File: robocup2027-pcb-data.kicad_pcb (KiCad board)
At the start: 4 copper layers, 83 x 117 mm, 52 parts, among them M5 Motor_Servo, M6 Motor_Servo, Q1 BPW40, Q2 BPW40, U1 ESP32-DEVKITC-32E

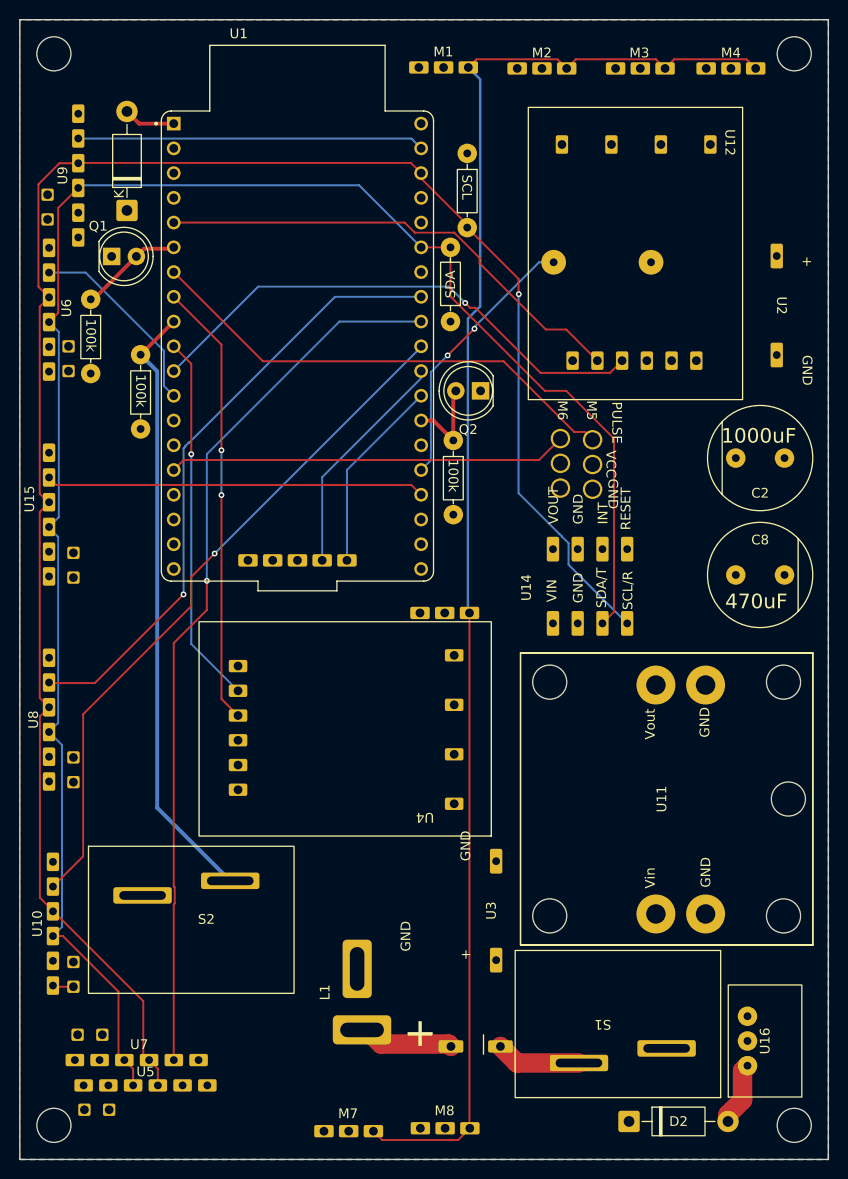
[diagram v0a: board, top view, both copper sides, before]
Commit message: fix: conflict between switches and cables
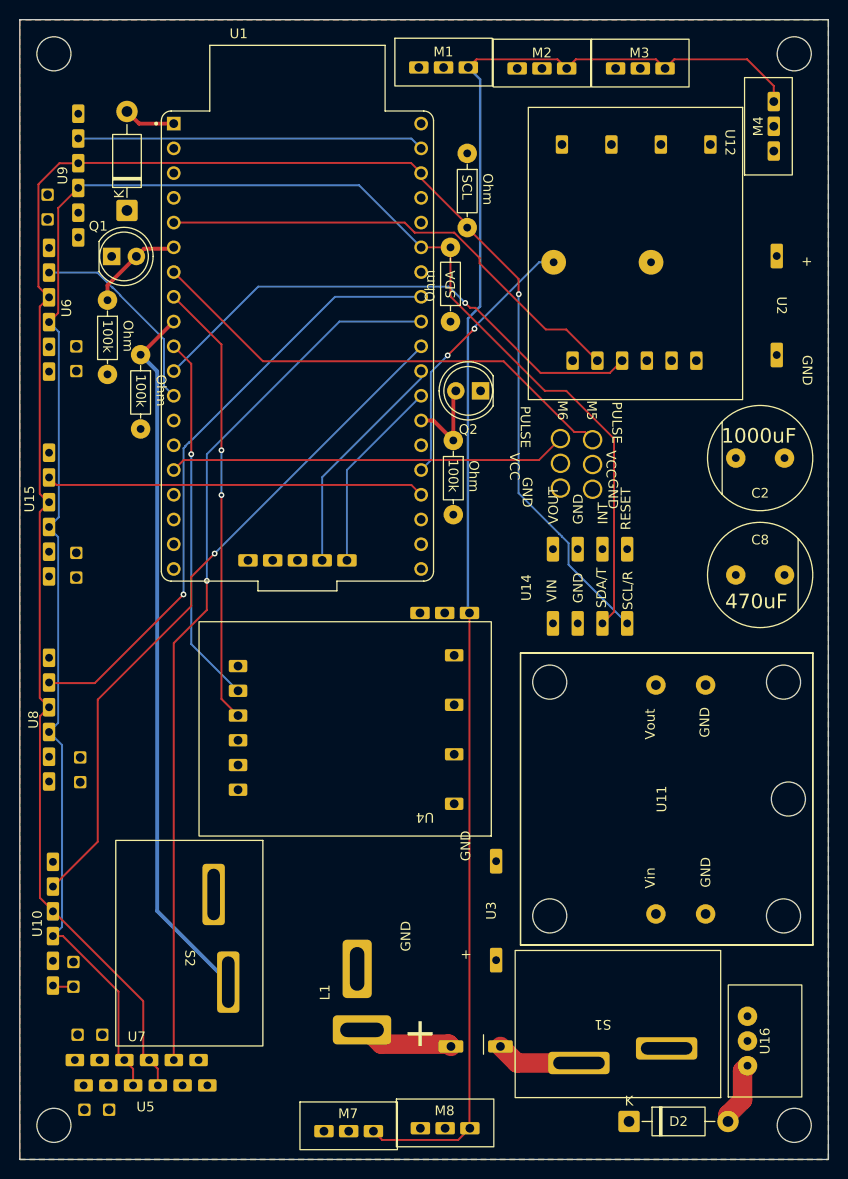
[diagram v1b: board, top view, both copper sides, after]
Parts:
- moved M4 7.39 mm to (167.4, 43.9), turned to 90 degrees
- moved S2 2.41 mm to (107.4, 127.8), turned to -90 degrees
- moved R4 1.73 mm to (99.0, 65.6)
- moved C3 0.80 mm to (95.8, 67.8)
- moved C5 0.70 mm to (96.2, 110.0)
- moved C4 0.30 mm to (95.8, 89.0)
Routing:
- net Net-(U1-IO25): track 62.6 -> 73.0 mm
- net STS3032_signal: track 152.6 -> 156.8 mm
- net photoresistor_1: track 10.7 -> 9.94 mm
- net XSHUT1: track 20.1 -> 20.9 mm

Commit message: remove: 6v voltmeter and Motor conector
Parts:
- removed M4: ~, robo:sts3032
- removed U2: ~, robo:voltmeter
- moved M1 0.10 mm to (133.5, 38.0)
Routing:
- net STS3032_signal: track 156.8 -> 142.5 mm

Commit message: refactor: motor connector, capacitor
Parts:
- removed Q1, Q2: BPW40, LED_THT:LED_D5.0mm_Clear
- removed R4, R5: 100k, robo:Resister
- moved S2 2.70 mm to (104.7, 127.8)
- moved C7 2.41 mm to (94.8, 137.4)
- moved M7 0.42 mm to (123.5, 146.8)
- turned C8 to 180 degrees
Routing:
- net photoresistor_2: track 9.85 -> 0.00 mm
- net photoresistor_1: track 9.94 -> 3.11 mm
- net Net-(U1-IO25): track 73.0 -> 71.7 mm

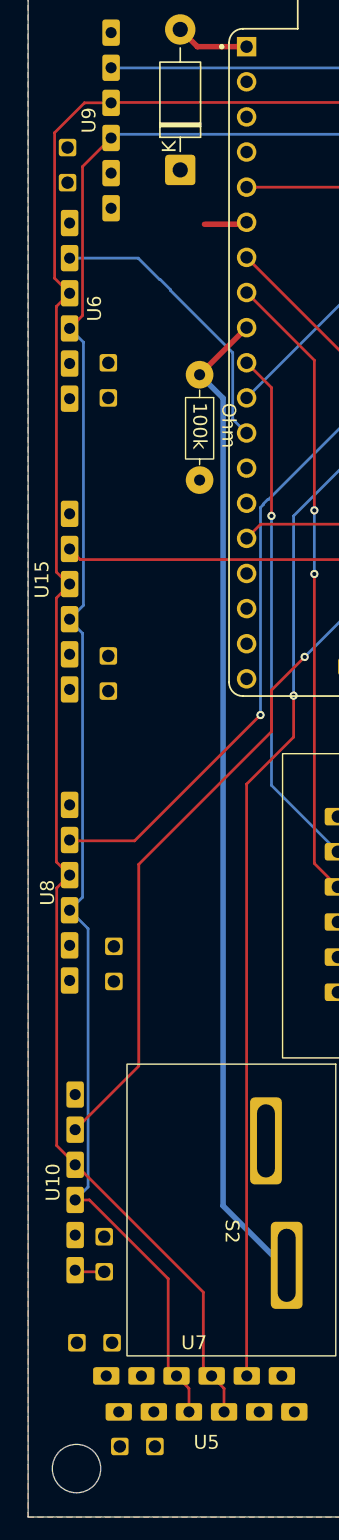
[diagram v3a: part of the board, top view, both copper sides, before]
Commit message: update: add xshout num on silkscreen
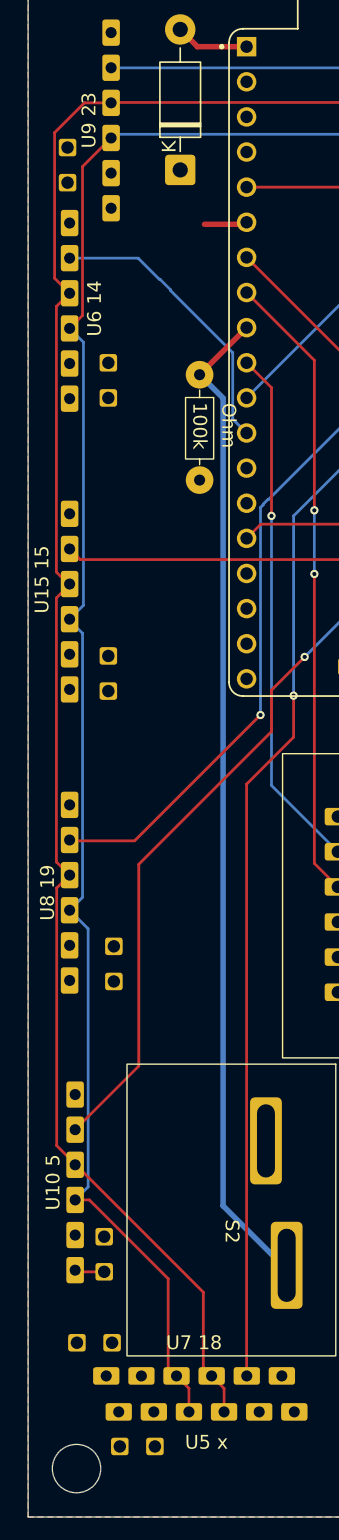
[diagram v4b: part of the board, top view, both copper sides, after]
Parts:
- U10 5: renamed from U10
- U15 15: renamed from U15
- U5 x: renamed from U5
- U6 14: renamed from U6
- U7 18: renamed from U7
- U8 19: renamed from U8
- U9 23: renamed from U9
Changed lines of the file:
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@@
 		(layer "F.Cu")
 		(at 93 83.8 90)
-		(property "Reference" "U15"
+		(property "Reference" "U15 15"
 			(at 1.6 -2 90)
 			(unlocked yes)
@@
 		(layer "F.Cu")
 		(at 102.9 142.4)
-		(property "Reference" "U5"
+		(property "Reference" "U5 x"
 			(at 0 2.2 0)
 			(unlocked yes)
@@
 		(layer "F.Cu")
 		(at 102 139.8)
-		(property "Reference" "U7"
+		(property "Reference" "U7 18"
 			(at 0 -2.4 0)
 			(unlocked yes)
@@
 		(layer "F.Cu")
 		(at 93 104.85 90)
-		(property "Reference" "U8"
+		(property "Reference" "U8 19"
 			(at 0 -1.6 90)
 			(unlocked yes)
@@
 		(layer "F.Cu")
 		(at 96 49 90)
-		(property "Reference" "U9"
+		(property "Reference" "U9 23"
 			(at 0.01 -1.6 90)
 			(unlocked yes)
@@
 		(layer "F.Cu")
 		(at 93 62.77 90)
-		(property "Reference" "U6"
+		(property "Reference" "U6 14"
 			(at 0.17 1.8 90)
 			(unlocked yes)
@@
 		(layer "F.Cu")
 		(at 93.4 125.8 90)
-		(property "Reference" "U10"
+		(property "Reference" "U10 5"
 			(at 0 -1.6 90)
 			(unlocked yes)

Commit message: update: pcb pullup
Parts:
- moved R3 7.70 mm to (102.5, 63.5)
- moved D1 1.08 mm to (101.0, 53.7)
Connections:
- R3 pad 1: Net-(U1-IO25) -> +3.3V
- R3 pad 2: GND -> Net-(U1-IO25)
- S2 pad 1: +3.3V -> Net-(U1-IO25)
- S2 pad 2: Net-(U1-IO25) -> GND
- U1 pad J2_6: photoresistor_1 -> unconnected-(U1-IO35-PadJ2_6)
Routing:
- net Net-(U1-IO25): track 71.7 -> 62.3 mm
- net photoresistor_1: track 3.11 -> 0.00 mm
